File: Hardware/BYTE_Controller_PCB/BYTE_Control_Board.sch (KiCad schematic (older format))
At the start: 9 parts, among them J1 8P8C_Shielded, Q1 2N7002, U1 SeeeduinoXIAO

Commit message: modify controller board
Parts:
- removed Q1: 2N7002, Package_TO_SOT_SMD:SOT-23, symbol Transistor_FET:2N7002
- removed R1, R2, R3, R4, R5, R6: R_US, Resistor_SMD:R_0603_1608Metric_Pad1.05x0.95mm_HandSolder, symbol Device:R_US
- removed U1: SeeeduinoXIAO, XIAO:Seeeduino XIAO-MOUDLE14P-2.54-21X17.8MM, symbol XIAO:SeeeduinoXIAO
- added C? (x2): 4.7uF, Capacitor_SMD:C_0603_1608Metric, symbol Device:C_Small
- added D? (x2): RED, LED_SMD:LED_0805_2012Metric, symbol Device:LED_Small
- added P?: USB_C_Plug_USB2.0, symbol Connector:USB_C_Plug_USB2.0
- added R? (x5): 2K, Resistor_SMD:R_0603_1608Metric, symbol Device:R_Small
- added U?: BL653, Controller:BL653_v5, symbol byteController:BL653
- added U?: MCP73830T-2AAI_MYY, Controller:2x2TDFN, symbol byteController:MCP73830T-2AAI_MYY
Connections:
- net labels added: +BATT, CC1, CC2, D+, D-, SCL, SDA, STAT, SWCLK, SWDIO, VBUS
- wire segments 42 -> 49
- no-connect marks 0 -> 1
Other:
- note added: "The MCP73830/L devices are always enabled with an\ninternal pull-down resistor. Pulling the CE pin high will\nenter Standby mode"
- moved on the sheet: J1

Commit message: update pcbs
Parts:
- P1: renamed from P?; footprint (none) -> Connectors:C393939
- gave numbers to parts that had none: 11
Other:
- moved on the sheet: U2
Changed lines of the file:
@@
 L power:GND #PWR0107
 U 1 1 5F44BFBD
-P 9760 4225
-F 0 "#PWR0107" H 9760 3975 50  0001 C CNN
-F 1 "GND" H 9765 4052 50  0000 C CNN
-F 2 "" H 9760 4225 50  0001 C CNN
-F 3 "" H 9760 4225 50  0001 C CNN
-	1    9760 4225
-	1    0    0    -1
-$EndComp
-$Comp
-L byteController:BL653 U?
+P 9760 4510
+F 0 "#PWR0107" H 9760 4260 50  0001 C CNN
+F 1 "GND" H 9765 4337 50  0000 C CNN
+F 2 "" H 9760 4510 50  0001 C CNN
+F 3 "" H 9760 4510 50  0001 C CNN
+	1    9760 4510
+	1    0    0    -1
+$EndComp
+$Comp
+L byteController:BL653 U2
 U 1 1 614AEB76
-P 9610 2370
-F 0 "U?" H 9095 3925 50  0000 C CNN
-F 1 "BL653" H 10365 625 50  0000 C CNN
-F 2 "Controller:BL653_v5" H 9610 1170 50  0001 C CNN
-F 3 "https://www.lairdconnect.com/documentation/datasheet-bl653-series" H 9560 1070 50  0001 C CNN
-	1    9610 2370
-	1    0    0    -1
-$EndComp
-Wire Wire Line
-	9760 4170 9760 4225
-Text Label 10925 3920 2    50   ~ 0
+P 9610 2655
+F 0 "U2" H 9095 4210 50  0000 C CNN
+F 1 "BL653" H 10365 910 50  0000 C CNN
+F 2 "Controller:BL653_v5" H 9610 1455 50  0001 C CNN
+F 3 "https://www.lairdconnect.com/documentation/datasheet-bl653-series" H 9560 1355 50  0001 C CNN
+	1    9610 2655
+	1    0    0    -1
+$EndComp
+Wire Wire Line
+	9760 4455 9760 4510
+Text Label 10925 4205 2    50   ~ 0
 SWCLK
 Wire Wire Line
-	10925 3920 10610 3920
-Text Label 10925 4020 2    50   ~ 0
+	10925 4205 10610 4205
+Text Label 10925 4305 2    50   ~ 0
 SWDIO
 Wire Wire Line
-	10925 4020 10610 4020
-Text Label 10790 2920 2    50   ~ 0
+	10925 4305 10610 4305
+Text Label 10790 3205 2    50   ~ 0
 D+
 Wire Wire Line
-	10790 2920 10610 2920
-Text Label 10790 3020 2    50   ~ 0
+	10790 3205 10610 3205
+Text Label 10790 3305 2    50   ~ 0
 D-
 Wire Wire Line
-	10790 3020 10610 3020
-$Comp
-L Connector:USB_C_Plug_USB2.0 P?
+	10790 3305 10610 3305
+$Comp
+L Connector:USB_C_Plug_USB2.0 P1
 U 1 1 614CD575
 P 1065 1610
-F 0 "P?" H 600 2270 50  0000 C CNN
+F 0 "P1" H 600 2270 50  0000 C CNN
 F 1 "USB_C_Plug_USB2.0" H 1445 860 50  0000 C CNN
-F 2 "" H 1215 1610 50  0001 C CNN
+F 2 "Connectors:C393939" H 1215 1610 50  0001 C CNN
 F 3 "https://www.usb.org/sites/default/files/documents/usb_type-c.zip" H 1215 1610 50  0001 C CNN
 	1    1065 1610
@@
 $EndComp
 $Comp
-L power:GND #PWR?
+L power:GND #PWR0101
 U 1 1 614D6657
 P 915 2665
-F 0 "#PWR?" H 915 2415 50  0001 C CNN
+F 0 "#PWR0101" H 915 2415 50  0001 C CNN
 F 1 "GND" H 920 2492 50  0000 C CNN
 F 2 "" H 915 2665 50  0001 C CNN
@@
 	1845 1210 1665 1210
 $Comp
-L power:VBUS #PWR?
+L power:VBUS #PWR0102
 U 1 1 614E606D
 P 1845 835
-F 0 "#PWR?" H 1845 685 50  0001 C CNN
+F 0 "#PWR0102" H 1845 685 50  0001 C CNN
 F 1 "VBUS" H 1860 1008 50  0000 C CNN
 F 2 "" H 1845 835 50  0001 C CNN
@@
 	1845 1010 1665 1010
 $Comp
-L byteController:MCP73830T-2AAI_MYY U?
+L byteController:MCP73830T-2AAI_MYY U1
 U 1 1 614ED8F7
 P 3660 1170
-F 0 "U?" H 3900 1300 50  0000 C CNN
+F 0 "U1" H 3900 1300 50  0000 C CNN
 F 1 "MCP73830T-2AAI_MYY" H 4690 620 50  0000 C CNN
 F 2 "Controller:2x2TDFN" H 4710 1270 50  0001 L CNN
@@
 $EndComp
 $Comp
-L power:+BATT #PWR?
+L power:+BATT #PWR0103
 U 1 1 614EFAB8
 P 5380 840
-F 0 "#PWR?" H 5380 690 50  0001 C CNN
+F 0 "#PWR0103" H 5380 690 50  0001 C CNN
 F 1 "+BATT" H 5395 1013 50  0000 C CNN
 F 2 "" H 5380 840 50  0001 C CNN
@@
 	5380 1170 4860 1170
 $Comp
-L power:GND #PWR?
+L power:GND #PWR0104
 U 1 1 614F1EEA
 P 4135 2000
-F 0 "#PWR?" H 4135 1750 50  0001 C CNN
+F 0 "#PWR0104" H 4135 1750 50  0001 C CNN
 F 1 "GND" H 4140 1827 50  0000 C CNN
 F 2 "" H 4135 2000 50  0001 C CNN
@@
 Connection ~ 4135 1935
 $Comp
-L power:VBUS #PWR?
+L power:VBUS #PWR0105
 U 1 1 614F43CC
 P 3360 845
-F 0 "#PWR?" H 3360 695 50  0001 C CNN
+F 0 "#PWR0105" H 3360 695 50  0001 C CNN
 F 1 "VBUS" H 3375 1018 50  0000 C CNN
 F 2 "" H 3360 845 50  0001 C CNN
@@
 	3360 845  3360 1170
 $Comp
-L Device:R_Small R?
+L Device:R_Small R2
 U 1 1 614F5BFE
 P 5380 1580
-F 0 "R?" H 5321 1534 50  0000 R CNN
+F 0 "R2" H 5321 1534 50  0000 R CNN
 F 1 "2K" H 5321 1625 50  0000 R CNN
 F 2 "Resistor_SMD:R_0603_1608Metric" H 5380 1580 50  0001 C CNN
@@
 	5380 1370 4860 1370
 $Comp
-L power:GND #PWR?
+L power:GND #PWR0106
 U 1 1 614F85EA
 P 5380 1785
-F 0 "#PWR?" H 5380 1535 50  0001 C CNN
+F 0 "#PWR0106" H 5380 1535 50  0001 C CNN
 F 1 "GND" H 5385 1612 50  0000 C CNN
 F 2 "" H 5380 1785 50  0001 C CNN
@@
 The MCP73830/L devices are always enabled with an\ninternal pull-down resistor. Pulling the CE pin high will\nenter Standby mode
 $Comp
-L Device:C_Small C?
+L Device:C_Small C2
 U 1 1 614FE9C8
 P 5785 1230
-F 0 "C?" H 5877 1276 50  0000 L CNN
+F 0 "C2" H 5877 1276 50  0000 L CNN
 F 1 "4.7uF" H 5877 1185 50  0000 L CNN
 F 2 "Capacitor_SMD:C_0603_1608Metric" H 5785 1230 50  0001 C CNN
@@
 $EndComp
 $Comp
-L power:+BATT #PWR?
+L power:+BATT #PWR0108
 U 1 1 614FF262
 P 5785 1065
-F 0 "#PWR?" H 5785 915 50  0001 C CNN
+F 0 "#PWR0108" H 5785 915 50  0001 C CNN
 F 1 "+BATT" H 5800 1238 50  0000 C CNN
 F 2 "" H 5785 1065 50  0001 C CNN
@@
 $EndComp
 $Comp
-L power:GND #PWR?
+L power:GND #PWR0109
 U 1 1 614FFC71
 P 5785 1430
-F 0 "#PWR?" H 5785 1180 50  0001 C CNN
+F 0 "#PWR0109" H 5785 1180 50  0001 C CNN
 F 1 "GND" H 5790 1257 50  0000 C CNN
 F 2 "" H 5785 1430 50  0001 C CNN
@@
 $EndComp
 $Comp
-L Device:C_Small C?
+L Device:C_Small C1
 U 1 1 61500A42
 P 2955 1030
-F 0 "C?" H 3047 1076 50  0000 L CNN
+F 0 "C1" H 3047 1076 50  0000 L CNN
 F 1 "4.7uF" H 3047 985 50  0000 L CNN
 F 2 "Capacitor_SMD:C_0603_1608Metric" H 2955 1030 50  0001 C CNN
@@
 $EndComp
 $Comp
-L power:VBUS #PWR?
+L power:VBUS #PWR0110
 U 1 1 61501632
 P 2955 845
-F 0 "#PWR?" H 2955 695 50  0001 C CNN
+F 0 "#PWR0110" H 2955 695 50  0001 C CNN
 F 1 "VBUS" H 2970 1018 50  0000 C CNN
 F 2 "" H 2955 845 50  0001 C CNN
@@
 $EndComp
 $Comp
-L power:GND #PWR?
+L power:GND #PWR0111
 U 1 1 615041FB
 P 2955 1190
-F 0 "#PWR?" H 2955 940 50  0001 C CNN
+F 0 "#PWR0111" H 2955 940 50  0001 C CNN
 F 1 "GND" H 2960 1017 50  0000 C CNN
 F 2 "" H 2955 1190 50  0001 C CNN
@@
 STAT
 $Comp
-L Device:LED_Small D?
+L Device:LED_Small D1
 U 1 1 61515176
 P 2450 1000
-F 0 "D?" V 2496 930 50  0000 R CNN
+F 0 "D1" V 2496 930 50  0000 R CNN
 F 1 "RED" V 2405 930 50  0000 R CNN
 F 2 "LED_SMD:LED_0805_2012Metric" V 2450 1000 50  0001 C CNN
@@
 $EndComp
 $Comp
-L Device:R_Small R?
+L Device:R_Small R1
 U 1 1 61516B35
 P 2450 1250
-F 0 "R?" H 2391 1204 50  0000 R CNN
+F 0 "R1" H 2391 1204 50  0000 R CNN
 F 1 "2K" H 2391 1295 50  0000 R CNN
 F 2 "Resistor_SMD:R_0603_1608Metric" H 2450 1250 50  0001 C CNN
@@
 	2450 1100 2450 1150
 $Comp
-L power:VBUS #PWR?
+L power:VBUS #PWR0112
 U 1 1 61518804
 P 2450 845
-F 0 "#PWR?" H 2450 695 50  0001 C CNN
+F 0 "#PWR0112" H 2450 695 50  0001 C CNN
 F 1 "VBUS" H 2465 1018 50  0000 C CNN
 F 2 "" H 2450 845 50  0001 C CNN
@@
 	2450 845  2450 900
 $Comp
-L Device:R_Small R?
+L Device:R_Small R3
 U 1 1 61534F4E
 P 6445 1135
-F 0 "R?" H 6580 1100 50  0000 R CNN
+F 0 "R3" H 6580 1100 50  0000 R CNN
 F 1 "2K" H 6595 1165 50  0000 R CNN
 F 2 "Resistor_SMD:R_0603_1608Metric" H 6445 1135 50  0001 C CNN
@@
 $EndComp
 $Comp
-L Device:R_Small R?
+L Device:R_Small R5
 U 1 1 615366F2
 P 6610 1140
-F 0 "R?" H 6551 1094 50  0000 R CNN
+F 0 "R5" H 6551 1094 50  0000 R CNN
 F 1 "2K" H 6551 1185 50  0000 R CNN
 F 2 "Resistor_SMD:R_0603_1608Metric" H 6610 1140 50  0001 C CNN
@@
 $EndComp
 $Comp
-L power:+BATT #PWR?
+L power:+BATT #PWR0113
 U 1 1 6153865B
 P 6445 880
-F 0 "#PWR?" H 6445 730 50  0001 C CNN
+F 0 "#PWR0113" H 6445 730 50  0001 C CNN
 F 1 "+BATT" H 6460 1053 50  0000 C CNN
 F 2 "" H 6445 880 50  0001 C CNN
@@
 STAT
 $Comp
-L Device:LED_Small D?
+L Device:LED_Small D2
 U 1 1 6155CE20
 P 6470 1915
-F 0 "D?" V 6516 1845 50  0000 R CNN
+F 0 "D2" V 6516 1845 50  0000 R CNN
 F 1 "RED" V 6425 1845 50  0000 R CNN
 F 2 "LED_SMD:LED_0805_2012Metric" V 6470 1915 50  0001 C CNN
@@
 $EndComp
 $Comp
-L Device:R_Small R?
+L Device:R_Small R4
 U 1 1 6155CE2A
 P 6470 2165
-F 0 "R?" H 6411 2119 50  0000 R CNN
+F 0 "R4" H 6411 2119 50  0000 R CNN
 F 1 "2K" H 6411 2210 50  0000 R CNN
 F 2 "Resistor_SMD:R_0603_1608Metric" H 6470 2165 50  0001 C CNN
@@
 	6470 1760 6470 1815
 $Comp
-L power:+BATT #PWR?
+L power:+BATT #PWR0114
 U 1 1 615671DE
 P 6470 1760
-F 0 "#PWR?" H 6470 1610 50  0001 C CNN
+F 0 "#PWR0114" H 6470 1610 50  0001 C CNN
 F 1 "+BATT" H 6485 1933 50  0000 C CNN
 F 2 "" H 6470 1760 50  0001 C CNN

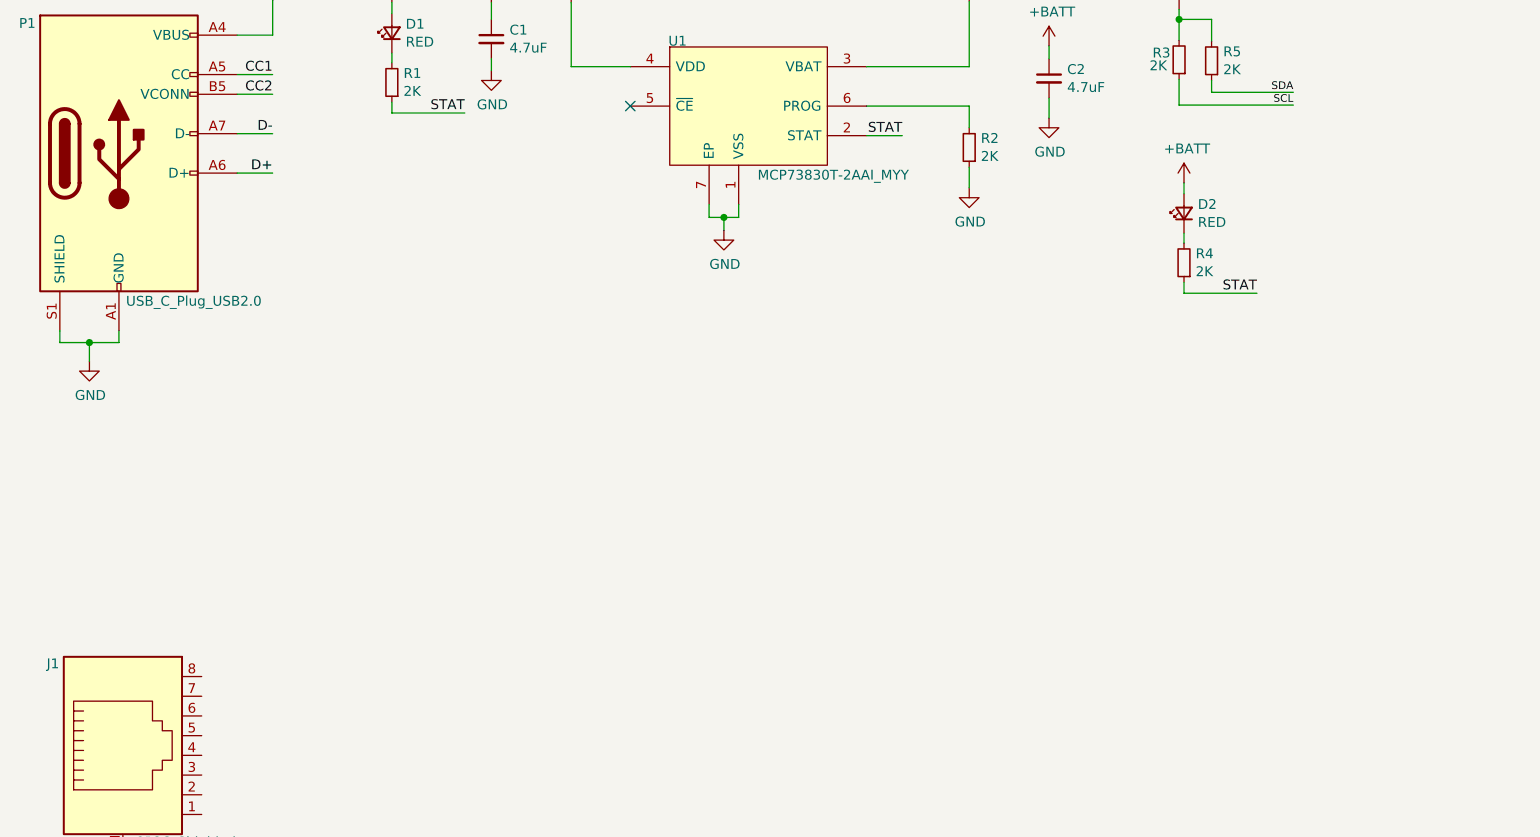
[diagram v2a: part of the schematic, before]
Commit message: update controller PCB added battery reading circuit
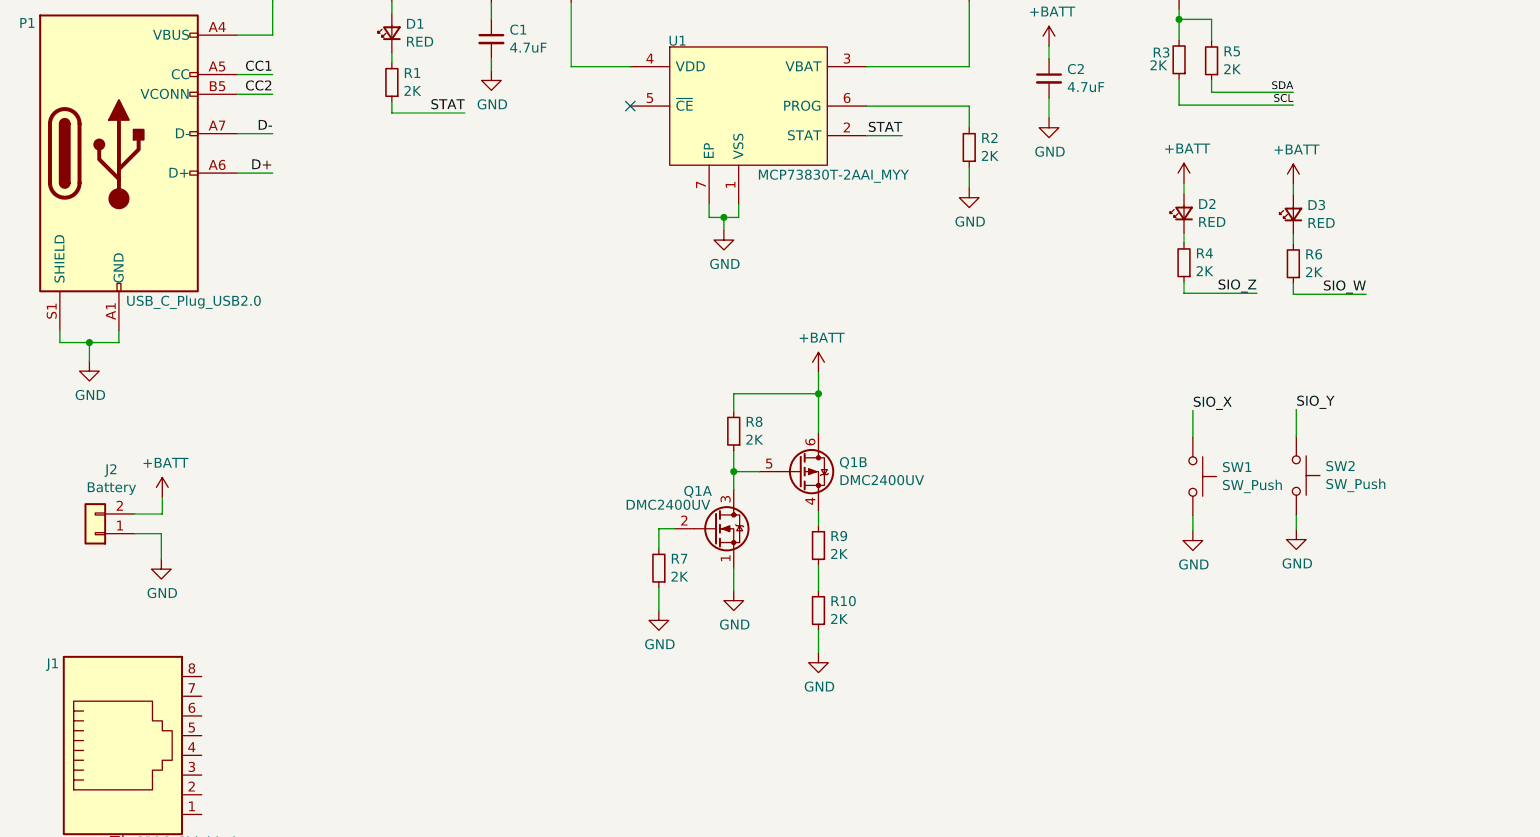
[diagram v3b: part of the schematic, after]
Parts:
- added D3: RED, LED_SMD:LED_0805_2012Metric, symbol Device:LED_Small
- added J2: Battery, Connector_PinHeader_2.54mm:PinHeader_1x02_P2.54mm_Vertical, symbol Connector_Generic:Conn_01x02
- added Q1: DMC2400UV, Package_TO_SOT_SMD:SOT-563, symbol byteController:DMC2400UV-Transistor_FET
- added R10, R6, R7, R8, R9: 2K, Resistor_SMD:R_0603_1608Metric, symbol Device:R_Small
- added SW1, SW2: SW_Push, Button_Switch_SMD:SW_SPST_TL3305A, symbol Switch:SW_Push
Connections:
- net +BATT: now also D3.2 (A), J2.2 (Pin_2), Q1.6 (D), R8.2
- net GND: now also J2.1 (Pin_1), Q1.1 (S2), R10.1, R7.1, SW1.2, SW2.2
- net STAT: no longer R4.1
- new net: D3.1 (K), R6.2
- new net: Q1.2 (G), R7.2
- new net: Q1.4 (S2), R9.2
- new net: Q1.3 (D), Q1.5 (G), R8.1
- new net: R10.2, R9.1
- new net SIO_W: R6.1
- new net SIO_X: SW1.1
- new net SIO_Y: SW2.1
- new net SIO_Z: R4.1

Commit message: update byte controller
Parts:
- added C3: 4.7uF, Capacitor_SMD:C_0603_1608Metric, symbol Device:C_Small
- added C4: 100nF, Capacitor_SMD:C_0603_1608Metric, symbol Device:C_Small
- added J3: Expansion, Connector_PinHeader_2.54mm:PinHeader_2x03_P2.54mm_Vertical, symbol Connector_Generic:Conn_02x03_Odd_Even
- added J4: SWD, Connector_PinHeader_2.54mm:PinHeader_1x04_P2.54mm_Vertical, symbol Connector_Generic:Conn_01x04
- added R11: 5.1K, Resistor_SMD:R_0603_1608Metric, symbol Device:R_Small
- added R12: 5.1k, Resistor_SMD:R_0603_1608Metric, symbol Device:R_Small
- added R13: 10K, Resistor_SMD:R_0603_1608Metric, symbol Device:R_Small
- added SW3: RST, Button_Switch_SMD:SW_Push_1P1T-SH_NO_CK_KMR2xxG, symbol Switch:SW_Push
- SW1, SW2: value SW_Push -> GPIO
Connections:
- net SIO_W is gone; now on net SIO_5: R6.1
- net SIO_X is gone; now on net SIO_20: SW1.1
- net SIO_Y is gone; now on net SIO_0: SW2.1
- net SIO_Z is gone; now on net SIO_1: R4.1
- net +BATT: now also J1.5, U2.25 (VDD_HV), C4.1, J3.2 (Pin_2), J4.1 (Pin_1), R13.2
- net CC1: now also R12.1
- net CC2: now also R11.2
- net GND: now also J1.7, J1.SH, C3.2, C4.2, J3.5 (Pin_5), J4.4 (Pin_4), R11.1, R12.2, SW3.2
- net SCL: now also J1.4, U2.5 (SIO_35), J3.6 (Pin_6)
- net SDA: now also J1.3, U2.7 (SIO_32), J3.4 (Pin_4)
- net SWCLK: now also J4.2 (Pin_2)
- net SWDIO: now also J4.3 (Pin_3)
- net VBUS: now also U2.24 (VBUS), C3.1
- net BYTE_SENSOR_1: now reaches J1.2
- net BYTE_SENSOR_1: now also U2.16 (SIO_17)
- net Sensor_INT: now reaches J1.6
- net Sensor_INT: now also U2.37 (SIO_07)
- net BYTE_SENSOR_2: now reaches J1.8
- net BYTE_SENSOR_2: now also U2.18 (SIO_15)
- net SIO_24: now reaches U2.10 (SIO_24)
- net SIO_24: now also J3.3 (Pin_3)
- net SIO_20: now reaches U2.13 (SIO_20)
- net RST: now reaches U2.19 (nRESET)
- net RST: now also R13.1, SW3.1
- net SIO_5: now reaches U2.39 (SIO_05/AIN3)
- net SIO_1: now reaches U2.41 (SIO_01)
- net SIO_0: now reaches U2.42 (SIO_00)
- net BATT_LVL_EN: now reaches U2.45 (SIO_30/AIN6)
- net BATT_LVL_EN: now also Q1.2 (G), R7.2
- net BATT_LVL: now reaches U2.49 (SIO_03/AIN1)
- net BATT_LVL: now also R10.2, R9.1
- net SIO_25: now reaches U2.8 (SIO_25)
- net SIO_25: now also J3.1 (Pin_1)
- no-connect marks 1 -> 33
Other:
- moved on the sheet: R3, R5
